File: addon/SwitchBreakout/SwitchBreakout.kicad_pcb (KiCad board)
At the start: 2 copper layers, 127.8 x 194.6 mm, 207 parts, among them IC1 SN74HCS72QPWRQ1, IC10 SN74HCS72QPWRQ1, IC11 SN74HCS72QPWRQ1, IC12 SN74HCS72QPWRQ1, IC13 SN74HCS72QPWRQ1, IC14 SN74HCS72QPWRQ1, IC15 SN74HCS72QPWRQ1, IC16 SN74HCS72QPWRQ1, IC2 SN74HCS72QPWRQ1, IC3 SN74HCS72QPWRQ1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

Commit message: Inter
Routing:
- net /G4: track 18.9 -> 144.9 mm, vias 0 -> 2
- net /D-Lach 9-16/BTN2: track 0.00 -> 69.5 mm, vias 0 -> 3
- net /D-Lach 9-16/BTN4: track 0.00 -> 49.2 mm
- net /D-Lach 9-16/BTN1: track 0.00 -> 48.7 mm, vias 0 -> 1
- net /D-Latch 17-24/D-Latch 4/CLK1: track 16.1 -> 56.9 mm
- net /B5: track 148.1 -> 140.2 mm
- net /B6: track 178.3 -> 170.9 mm
- net /D-Latch 1-8/BTN6: track 38.7 -> 32.7 mm
- net /B2: track 154.1 -> 148.2 mm
- net /D-Latch 25-32/D-Latch 2/BTN2: track 90.2 -> 95.1 mm
- net /G8: track 156.0 -> 151.3 mm
- net /D-Latch 17-24/D-Latch 0/BTN2: track 107.6 -> 103.3 mm
- net /E1: track 80.8 -> 85.0 mm
- net /D4: track 235.3 -> 239.3 mm
- net /E5: track 99.5 -> 96.0 mm
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
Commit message: Morish
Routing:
- net /D-Lach 9-16/BTN3: track 0.00 -> 61.9 mm, vias 0 -> 1
- net /D-Lach 9-16/BTN8: track 0.00 -> 57.3 mm
- net /D-Lach 9-16/BTN7: track 0.00 -> 43.7 mm
- net /D-Lach 9-16/BTN5: track 0.00 -> 43.5 mm
- net /D-Lach 9-16/BTN6: track 0.00 -> 42.4 mm, vias 0 -> 1
- net /D-Latch 17-24/D-Latch 4/CLK1: track 56.9 -> 16.1 mm
- net /D-Latch 17-24/D-Latch 0/BTN2: track 103.3 -> 66.3 mm
- net /D-Lach 9-16/BTN4: track 49.2 -> 82.0 mm, vias 0 -> 2
- net /D-Latch 17-24/D-Latch 0/CLK2: track 25.6 -> 33.4 mm
- net /C6: track 216.2 -> 208.7 mm
- net /B8: track 186.9 -> 194.0 mm
- net /D1: track 184.0 -> 187.8 mm
- net /C1: track 159.3 -> 163.0 mm
- net /C2: track 171.2 -> 174.5 mm
- net /D-Lach 9-16/BTN1: track 48.7 -> 47.0 mm
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
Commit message: Cross
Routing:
- net /D-Latch 17-24/D-Latch 4/CLK1: track 16.1 -> 70.5 mm
- net /D-Latch 17-24/D-Latch 4/CLK2: track 28.7 -> 74.6 mm
- net /D-Latch 17-24/D-Latch 2/CLK2: track 24.5 -> 56.1 mm
- net /D-Latch 17-24/D-Latch 2/CLK1: track 16.1 -> 47.6 mm
- net /D-Latch 17-24/D-Latch 0/BTN1: track 68.6 -> 38.9 mm
- net /D-Latch 17-24/D-Latch 1/BTN1: track 62.5 -> 33.0 mm
- net /D-Latch 17-24/D-Latch 1/BTN2: track 60.2 -> 35.5 mm
- net /D-Latch 17-24/D-Latch 2/BTN1: track 53.0 -> 28.4 mm
- net /P8: track 77.8 -> 102.0 mm, vias 2 -> 3
- net /M8: track 202.4 -> 179.4 mm
- net /M6: track 214.2 -> 192.0 mm
- net /P5: track 73.8 -> 53.7 mm
- net /D-Latch 17-24/D-Latch 0/CLK2: track 33.4 -> 13.4 mm
- net /M5: track 190.8 -> 172.1 mm
- net /D-Latch 17-24/D-Latch 2/BTN2: track 48.3 -> 31.2 mm
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
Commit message: Wired
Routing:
- net GND: track 109.8 -> 194.3 mm, vias 10 -> 77
- net /D-Latch 1-8/D-Latch 2/CLK1: track 16.1 -> 80.3 mm, vias 0 -> 1
- net /D-Latch 1-8/D-Latch 2/CLK2: track 24.5 -> 78.5 mm, vias 0 -> 2
- net /D-Latch 1-8/D-Latch 4/CLK1: track 16.0 -> 56.8 mm, vias 0 -> 1
- net /D-Latch 1-8/D-Latch 0/CLK1: track 16.2 -> 53.8 mm, vias 0 -> 3
- net /D-Latch 1-8/D-Latch 4/CLK2: track 24.4 -> 59.7 mm, vias 0 -> 1
- net /D-Latch 1-8/D-Latch 1/CLK1: track 16.1 -> 50.8 mm, vias 0 -> 2
- net /D-Latch 17-24/D-Latch 0/BTN1: track 38.9 -> 73.2 mm, vias 0 -> 2
- net /D-Latch 17-24/D-Latch 0/CLK2: track 13.4 -> 47.5 mm, vias 0 -> 4
- net /D-Latch 1-8/D-Latch 0/CLK2: track 24.5 -> 55.1 mm, vias 0 -> 2
- net /D-Latch 17-24/D-Latch 1/BTN1: track 33.0 -> 62.5 mm, vias 0 -> 1
- net /D-Latch 1-8/D-Latch 1/CLK2: track 24.5 -> 53.4 mm, vias 0 -> 1
- net /M8: track 179.4 -> 206.9 mm
- net /D-Latch 17-24/D-Latch 1/BTN2: track 35.5 -> 60.5 mm, vias 0 -> 2
- net /D-Latch 17-24/D-Latch 2/BTN1: track 28.4 -> 53.0 mm, vias 0 -> 1
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- added copper zone on B.Cu, net GND

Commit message: Fixer upper
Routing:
- net VCC: track 35.8 -> 358.1 mm, vias 0 -> 123
- net GND: track 194.3 -> 267.5 mm, vias 77 -> 270
- net /D-Lach 9-16/BTN7: track 43.7 -> 101.6 mm, vias 0 -> 2
- net /D-Lach 9-16/BTN8: track 57.3 -> 114.0 mm, vias 0 -> 2
- net /D-Lach 9-16/BTN6: track 42.4 -> 93.7 mm, vias 1 -> 3
- net /D-Lach 9-16/BTN5: track 43.5 -> 84.6 mm, vias 0 -> 2
- net /D-Latch 1-8/BTN7: track 0.00 -> 26.8 mm, vias 0 -> 2
- net /D5: track 198.7 -> 214.4 mm
- net /D4: track 239.3 -> 254.6 mm
- net /D-Latch 1-8/BTN5: track 46.9 -> 59.4 mm
- net /D-Latch 1-8/BTN6: track 31.9 -> 43.1 mm
- net /C1: track 163.9 -> 172.5 mm
- net /D-Lach 9-16/BTN4: track 75.1 -> 83.5 mm
- net /D-Latch 1-8/D-Latch 4/BTN2: track 79.4 -> 87.6 mm
- net /C4: track 178.1 -> 186.2 mm
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- added copper zone on B.Cu, net VCC
- added copper zone on F.Cu, net VCC

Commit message: More fixes
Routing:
- net Net-(F5-Pad2): track 19.8 -> 16.0 mm
- net /J1: track 204.3 -> 205.8 mm
- net /J2: track 198.4 -> 199.7 mm
- net /L2: track 118.3 -> 119.0 mm
- net /O8: track 117.1 -> 117.8 mm, vias 5 -> 4
- net GND: vias 270 -> 306

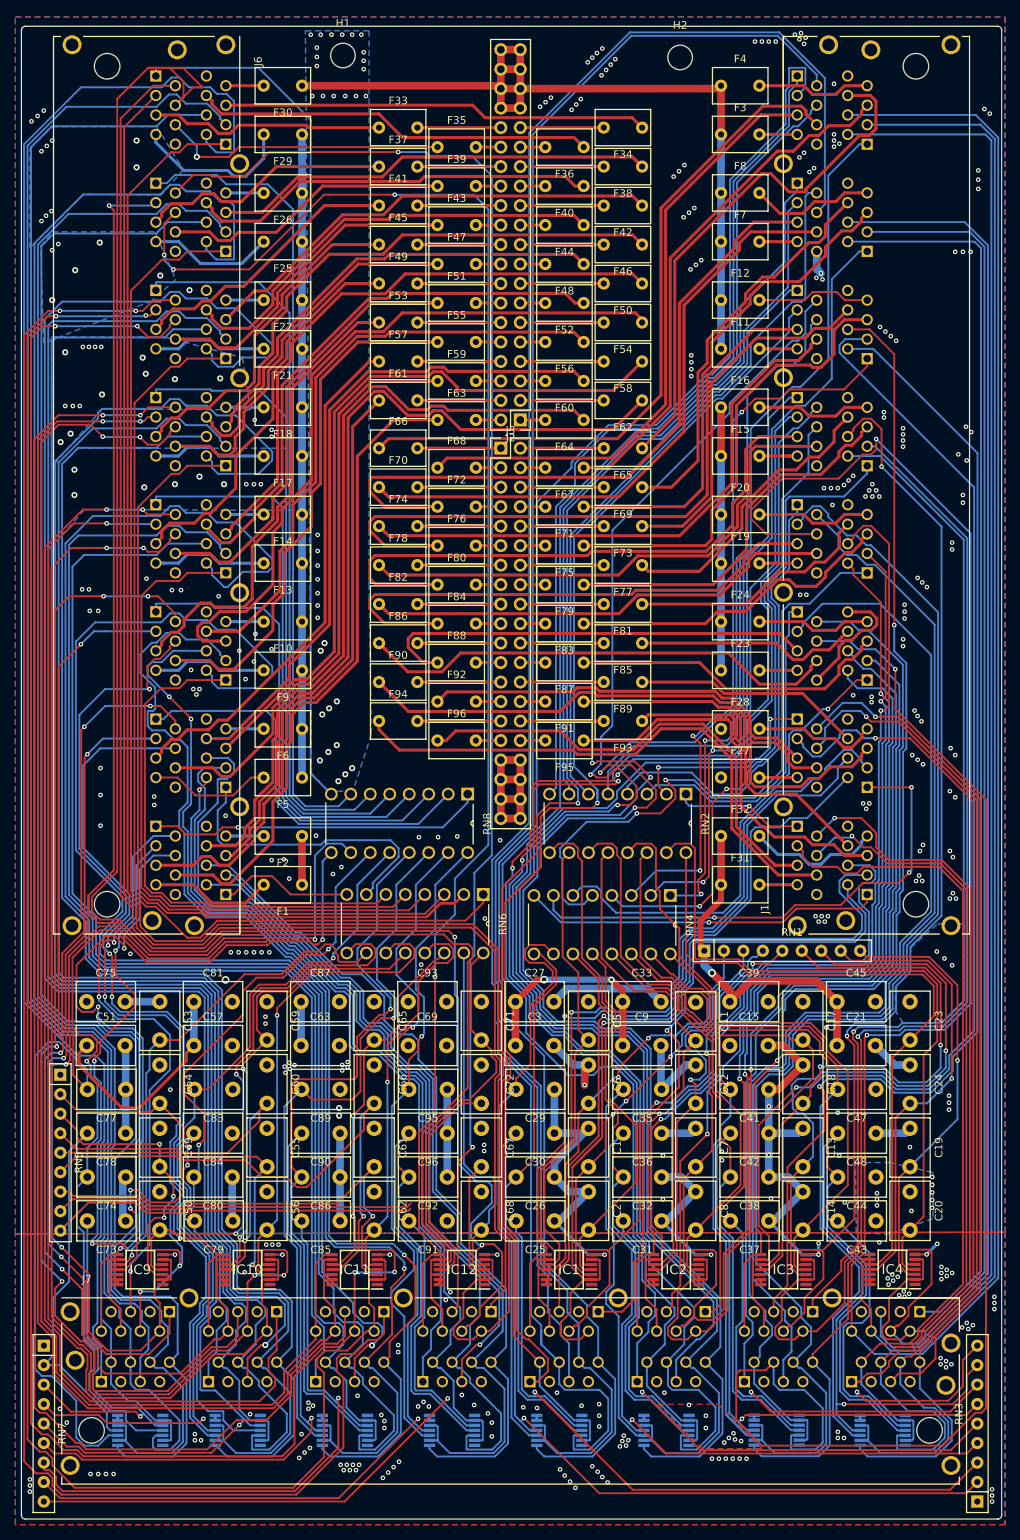
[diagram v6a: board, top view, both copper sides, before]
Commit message: Fix power rails
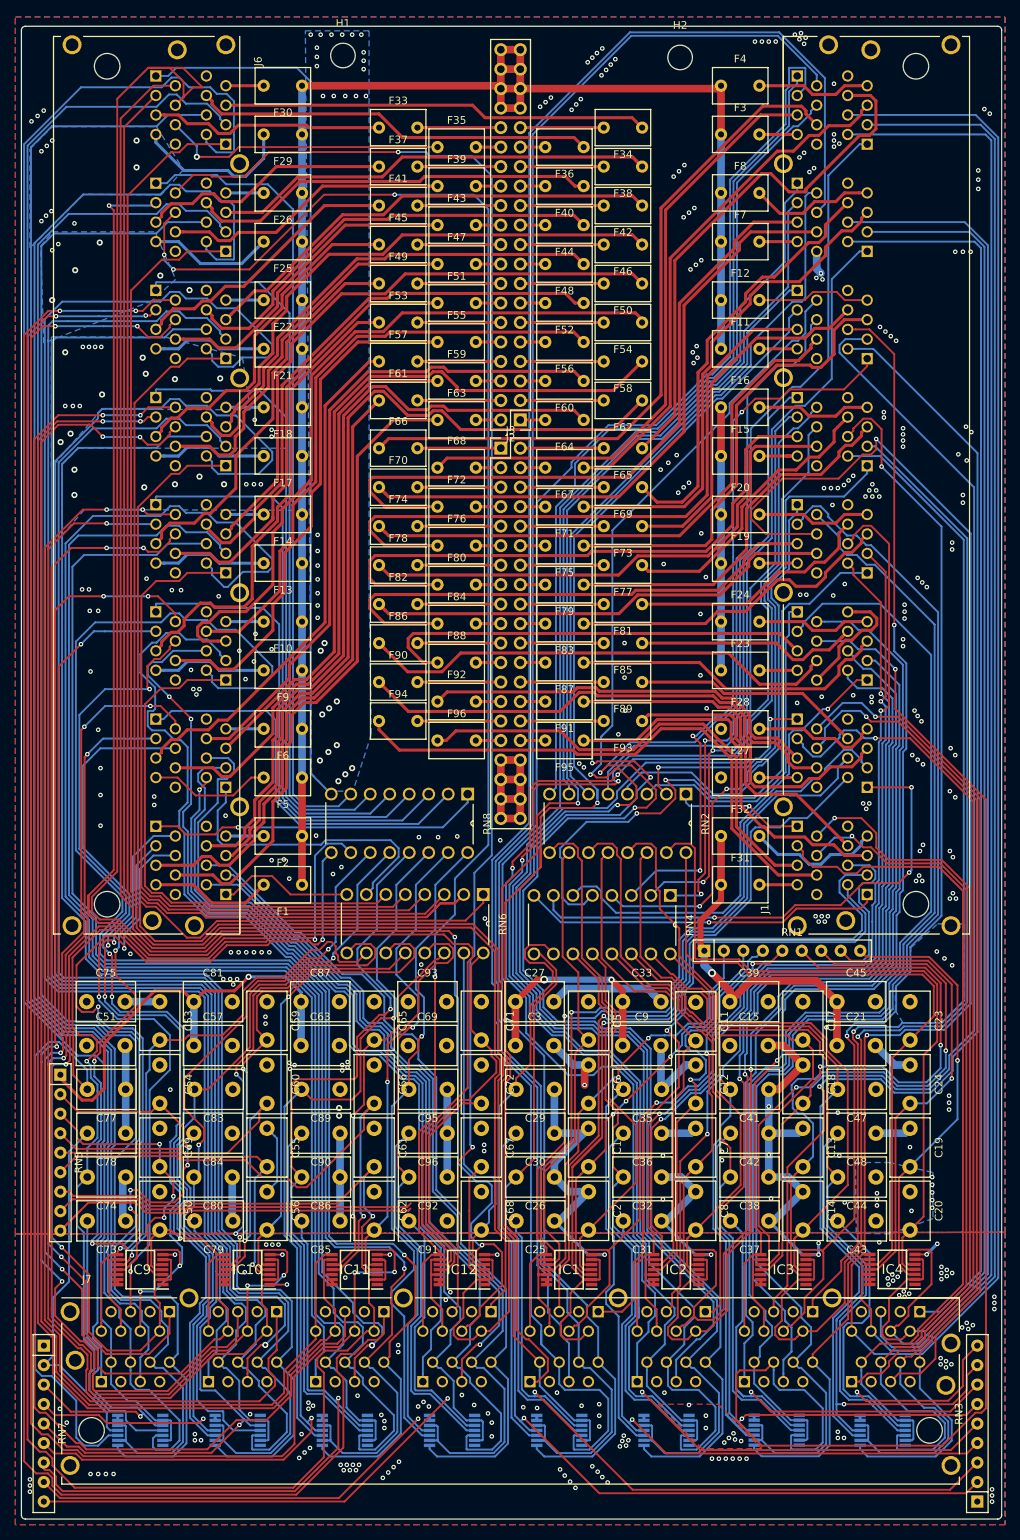
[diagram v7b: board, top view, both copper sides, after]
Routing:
- net VCC: track 358.1 -> 396.6 mm, vias 123 -> 126
- net GND: track 267.5 -> 276.8 mm, vias 306 -> 331
- net Net-(F69-Pad1): track 52.1 -> 55.7 mm
- net /D-Latch 25-32/BTN1: track 113.0 -> 115.3 mm
- net /D-Latch 17-24/D-Latch 0/BTN2: track 66.3 -> 68.6 mm
- net /D-Latch 17-24/D-Latch 1/BTN1: track 62.5 -> 64.3 mm
